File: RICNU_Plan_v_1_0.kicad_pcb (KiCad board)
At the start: 4 copper layers, 50 x 55 mm, 220 parts, among them J1 USB_OTG, J2 MOLEX-PC6, J3 DF52-4S-0.8H(21), J4 DF52-4S-0.8H(21), J5 MOLEX-PC20, J6 2x0.1, J7 FH19C-6S-0.5SH(05), Q1 N-CH, Q2 N-CH, SW1 CL-SB-12B-01T, SW2 SW_Push, SW3 SW_Push, U1 TPS2113, U2 TLV62568, U3 SN74AHC126, U4 FT232RL, U5 TCAN334G, U6 SN65HVD75, U7 BT121, U8 STM32F103RC, Y1 Crystal

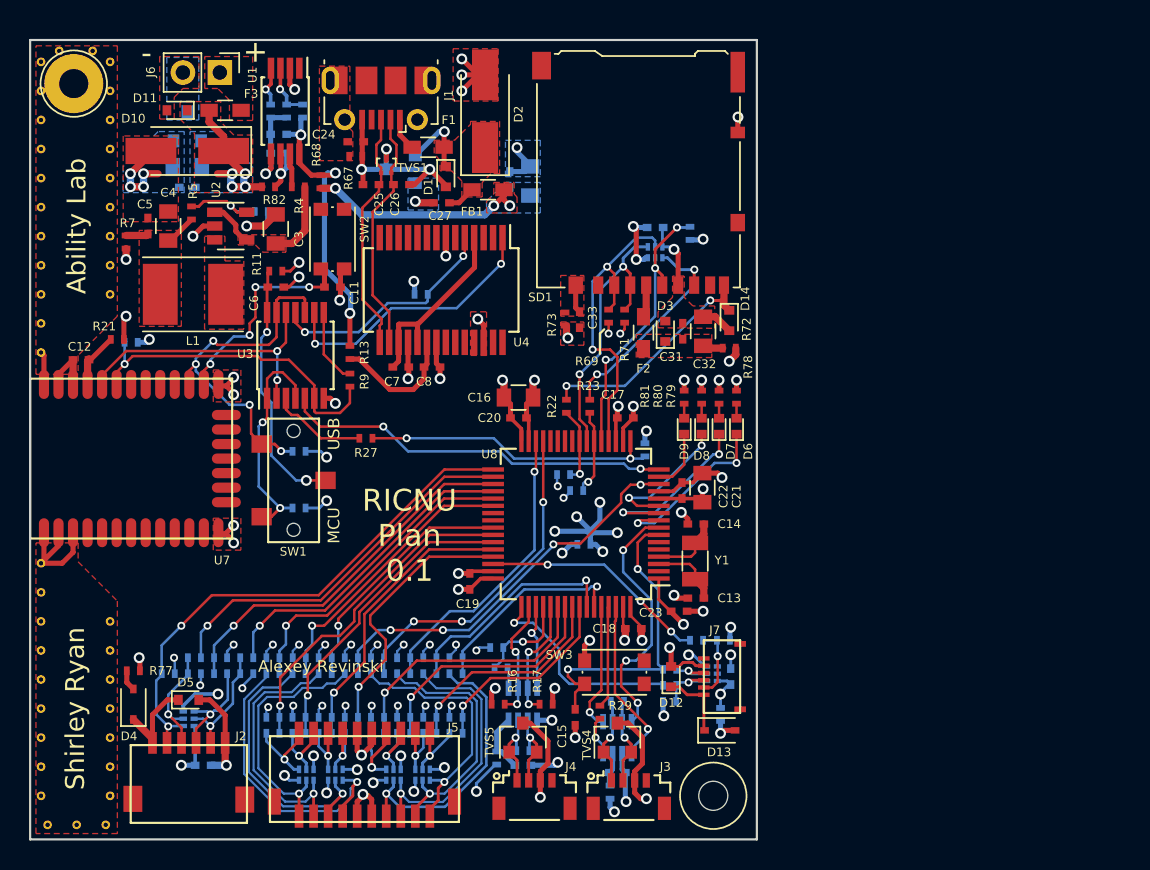
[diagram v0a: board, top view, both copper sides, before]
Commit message: Re-routed CAN, RS-485, and debug connectors (wrong polarity in all)
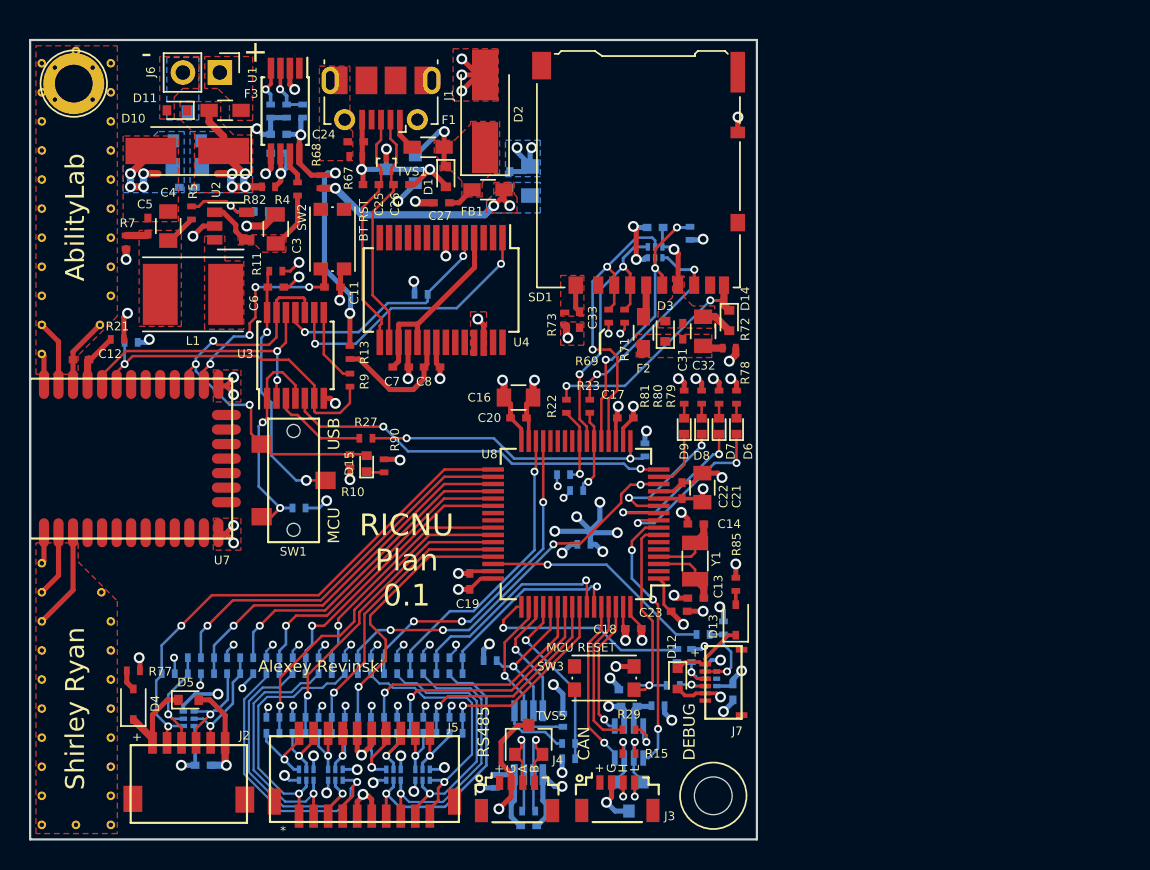
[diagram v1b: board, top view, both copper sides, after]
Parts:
- removed the REF** at (122.3, 94.5)
- removed the REF** at (127.1, 82.5)
- removed the REF** at (127.1, 84.5)
- removed the REF** at (127.1, 86.5)
- removed the REF** at (122.3, 86.5)
- removed the REF** at (122.3, 82.5)
- removed the REF** at (122.3, 84.5)
- removed the REF** at (127.1, 92.5)
- removed the REF** at (127.1, 94.5)
- removed the REF** at (127.1, 88.5)
- removed the REF** at (127.1, 90.5)
- removed the REF** at (122.3, 92.5)
- removed the REF** at (127.1, 78.5)
- removed the REF** at (122.3, 98.5)
- removed the REF** at (122.3, 96.5)
- removed the REF** at (122.3, 113.0)
- removed the REF** at (127.1, 117.0)
- removed the REF** at (127.1, 119.0)
- removed the REF** at (127.1, 129.0)
- removed the REF** at (127.1, 127.0)
- removed the REF** at (127.1, 125.0)
- removed the REF** at (127.1, 123.0)
- removed the REF** at (122.3, 90.5)
- removed the REF** at (127.1, 121.0)
- removed the REF** at (126.8, 131.0)
- removed the REF** at (124.8, 131.0)
- removed the REF** at (122.8, 131.0)
- removed the REF** at (122.3, 129.0)
- removed the REF** at (122.3, 127.0)
- removed the REF** at (122.3, 125.0)
- removed the REF** at (122.3, 123.0)
- removed the REF** at (122.3, 121.0)
- removed the REF** at (122.3, 119.0)
- removed the REF** at (122.3, 88.5)
- removed the REF** at (122.3, 117.0)
- removed the REF** at (122.3, 115.0)
- removed the REF** at (122.3, 78.5)
- removed the REF** at (122.3, 80.5)
- removed the REF** at (123.6, 77.8)
- removed the REF** at (125.9, 77.8)
- removed the REF** at (127.1, 80.5)
- added D15: LED, LEDs:LED_0402, F.Cu at (144.8, 106.2)
- added R90: R, Resistors_SMD:R_0402_NoSilk, F.Cu at (145.9, 106.3)
- added REF**: VIA-0.6-0.3, RICNU_Plan_v_1_0:VIA-0.6-0.3, F.Cu at (123.3, 81.1)
- added REF**: VIA-0.6-0.3, RICNU_Plan_v_1_0:VIA-0.6-0.3, F.Cu at (127.2, 92.6)
- added REF**: VIA-0.6-0.3, RICNU_Plan_v_1_0:VIA-0.6-0.3, F.Cu at (127.2, 94.6)
- added REF**: VIA-0.6-0.3, RICNU_Plan_v_1_0:VIA-0.6-0.3, F.Cu at (127.2, 90.6)
- added REF**: VIA-0.6-0.3, RICNU_Plan_v_1_0:VIA-0.6-0.3, F.Cu at (127.2, 86.6)
- added REF**: VIA-0.6-0.3, RICNU_Plan_v_1_0:VIA-0.6-0.3, F.Cu at (127.2, 88.6)
- added REF**: VIA-0.6-0.3, RICNU_Plan_v_1_0:VIA-0.6-0.3, F.Cu at (122.4, 78.6)
- added REF**: VIA-0.6-0.3, RICNU_Plan_v_1_0:VIA-0.6-0.3, F.Cu at (127.2, 78.6)
- added REF**: VIA-0.6-0.3, RICNU_Plan_v_1_0:VIA-0.6-0.3, F.Cu at (127.2, 80.6)
- added REF**: VIA-0.6-0.3, RICNU_Plan_v_1_0:VIA-0.6-0.3, F.Cu at (122.4, 98.6)
- added REF**: VIA-0.6-0.3, RICNU_Plan_v_1_0:VIA-0.6-0.3, F.Cu at (122.4, 96.6)
- added REF**: VIA-0.6-0.3, RICNU_Plan_v_1_0:VIA-0.6-0.3, F.Cu at (125.9, 81.1)
- added REF**: VIA-0.6-0.3, RICNU_Plan_v_1_0:VIA-0.6-0.3, F.Cu at (122.4, 94.6)
- added REF**: VIA-0.6-0.3, RICNU_Plan_v_1_0:VIA-0.6-0.3, F.Cu at (122.4, 92.6)
- added REF**: VIA-0.6-0.3, RICNU_Plan_v_1_0:VIA-0.6-0.3, F.Cu at (122.4, 90.6)
- added REF**: VIA-0.6-0.3, RICNU_Plan_v_1_0:VIA-0.6-0.3, F.Cu at (122.4, 84.6)
- added REF**: VIA-0.6-0.3, RICNU_Plan_v_1_0:VIA-0.6-0.3, F.Cu at (122.4, 82.6)
- added REF**: VIA-0.6-0.3, RICNU_Plan_v_1_0:VIA-0.6-0.3, F.Cu at (122.4, 86.6)
- added REF**: VIA-0.6-0.3, RICNU_Plan_v_1_0:VIA-0.6-0.3, F.Cu at (122.4, 88.6)
- added REF**: VIA-0.6-0.3, RICNU_Plan_v_1_0:VIA-0.6-0.3, F.Cu at (122.4, 80.6)
- added REF**: VIA-0.6-0.3, RICNU_Plan_v_1_0:VIA-0.6-0.3, F.Cu at (124.8, 131.0)
- added REF**: VIA-0.6-0.3, RICNU_Plan_v_1_0:VIA-0.6-0.3, F.Cu at (127.2, 131.0)
- added REF**: VIA-0.6-0.3, RICNU_Plan_v_1_0:VIA-0.6-0.3, F.Cu at (123.3, 78.9)
- added REF**: VIA-0.6-0.3, RICNU_Plan_v_1_0:VIA-0.6-0.3, F.Cu at (127.2, 129.0)
- added REF**: VIA-0.6-0.3, RICNU_Plan_v_1_0:VIA-0.6-0.3, F.Cu at (127.2, 127.0)
- added REF**: VIA-0.6-0.3, RICNU_Plan_v_1_0:VIA-0.6-0.3, F.Cu at (127.2, 125.0)
- added REF**: VIA-0.6-0.3, RICNU_Plan_v_1_0:VIA-0.6-0.3, F.Cu at (127.2, 123.0)
- added REF**: VIA-0.6-0.3, RICNU_Plan_v_1_0:VIA-0.6-0.3, F.Cu at (127.2, 121.0)
- added REF**: VIA-0.6-0.3, RICNU_Plan_v_1_0:VIA-0.6-0.3, F.Cu at (127.2, 119.0)
- added REF**: VIA-0.6-0.3, RICNU_Plan_v_1_0:VIA-0.6-0.3, F.Cu at (127.2, 117.0)
- added REF**: VIA-0.6-0.3, RICNU_Plan_v_1_0:VIA-0.6-0.3, F.Cu at (126.5, 115.0)
- added REF**: VIA-0.6-0.3, RICNU_Plan_v_1_0:VIA-0.6-0.3, F.Cu at (122.4, 131.0)
- added REF**: VIA-0.6-0.3, RICNU_Plan_v_1_0:VIA-0.6-0.3, F.Cu at (122.4, 129.0)
- added REF**: VIA-0.6-0.3, RICNU_Plan_v_1_0:VIA-0.6-0.3, F.Cu at (125.9, 78.9)
- added REF**: VIA-0.6-0.3, RICNU_Plan_v_1_0:VIA-0.6-0.3, F.Cu at (122.4, 127.0)
- added REF**: VIA-0.6-0.3, RICNU_Plan_v_1_0:VIA-0.6-0.3, F.Cu at (122.4, 125.0)
- added REF**: VIA-0.6-0.3, RICNU_Plan_v_1_0:VIA-0.6-0.3, F.Cu at (122.4, 123.0)
- added REF**: VIA-0.6-0.3, RICNU_Plan_v_1_0:VIA-0.6-0.3, F.Cu at (122.4, 121.0)
- added REF**: VIA-0.6-0.3, RICNU_Plan_v_1_0:VIA-0.6-0.3, F.Cu at (122.4, 119.0)
- added REF**: VIA-0.6-0.3, RICNU_Plan_v_1_0:VIA-0.6-0.3, F.Cu at (122.4, 117.0)
- added REF**: VIA-0.6-0.3, RICNU_Plan_v_1_0:VIA-0.6-0.3, F.Cu at (122.4, 115.0)
- added REF**: VIA-0.6-0.3, RICNU_Plan_v_1_0:VIA-0.6-0.3, F.Cu at (122.4, 113.0)
- added REF**: VIA-0.6-0.3, RICNU_Plan_v_1_0:VIA-0.6-0.3, F.Cu at (126.4, 96.6)
- added REF**: VIA-0.6-0.3, RICNU_Plan_v_1_0:VIA-0.6-0.3, F.Cu at (124.8, 77.8)
- added REF**: VIA-0.6-0.3, RICNU_Plan_v_1_0:VIA-0.6-0.3, F.Cu at (127.2, 84.6)
- added REF**: VIA-0.6-0.3, RICNU_Plan_v_1_0:VIA-0.6-0.3, F.Cu at (127.2, 82.6)
- C15, R16, R17, TVS4: moved to B.Cu
- R10, R15, R85: moved to F.Cu
- SW2, SW3: value SW_Push -> SW_Push_4pin; footprint Buttons_Switches_SMD:SW_SPST_KMR2 -> RICNU_Plan_v_1_0:SW_SPST_KMR7
- U6: footprint TO_SOT_Packages_SMD:SOT-23-8 -> Housings_SSOP:VSSOP-8_3.0x3.0mm_Pitch0.65mm
- moved R86 9.11 mm to (158.7, 126.5)
- moved R85 9.01 mm to (170.2, 114.5)
- moved D13 7.68 mm to (170.2, 116.9), turned to 90 degrees
- moved R28 6.98 mm to (158.7, 125.4), turned to 0 degrees
- moved R14 6.80 mm to (164.8, 122.8), turned to 180 degrees
- moved R17 4.88 mm to (153.2, 119.7), turned to 0 degrees
- moved C9 4.62 mm to (162.8, 122.8), turned to 180 degrees
- moved R16 4.58 mm to (158.2, 123.8), turned to 90 degrees
- moved C10 4.17 mm to (155.9, 131.1)
- moved R19 4.17 mm to (155.9, 130.1)
- moved TVS4 4.13 mm to (162.8, 129.1), turned to 270 degrees
- moved C15 4.03 mm to (162.7, 121.7), turned to 180 degrees
- moved R15 3.69 mm to (162.8, 126.1), turned to 0 degrees
- moved R10 3.56 mm to (143.6, 106.0), turned to 270 degrees
- moved R84 3.49 mm to (167.1, 119.3), turned to 90 degrees
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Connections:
- J3 pad 1: /CAN- -> Net-(J3-Pad1)
- J3 pad 2: /CAN+ -> GND
- J3 pad 3: GND -> /CAN+
- J3 pad 4: Net-(J3-Pad4) -> /CAN-
- J4 pad 1: /RS485_D- -> Net-(J4-Pad1)
- J4 pad 2: /RS485_D+ -> GND
- J4 pad 3: GND -> /RS485_D+
- J4 pad 4: Net-(J4-Pad4) -> /RS485_D-
- J7 pad 1: /Debug Connector/SWD_VREF -> Net-(J7-Pad1)
- J7 pad 2: /SWD_SWDIO -> GND
- J7 pad 3: /SWD_SWCLK -> /SWD_RESET
- J7 pad 4: /SWD_RESET -> /SWD_SWCLK
- J7 pad 5: GND -> /SWD_SWDIO
- J7 pad 6: Net-(J7-Pad6) -> /Debug Connector/SWD_VREF
- R19 pad 1: /RS485_D- -> /RS485_D+
- R19 pad 2: /RS485_D+ -> /RS485_D-
- TVS10 pad 1: /SWD_SWCLK -> /SWD_RESET
- TVS10 pad 2: /SWD_RESET -> /SWD_SWCLK
- TVS4 pad 1: /CAN- -> /CAN+
- TVS4 pad 2: /CAN+ -> /CAN-
- TVS5 pad 1: /RS485_D- -> /RS485_D+
- TVS5 pad 2: /RS485_D+ -> /RS485_D-
- U6 pad 6: /RS485_D+ -> /RS485_D-
- U6 pad 7: /RS485_D- -> /RS485_D+
- U8 pad 60: /CAN_SHDN -> /CAN_STB
- U8 pad 8: /CAN_STB -> /CAN_SHDN
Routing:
- net GND: track 147.7 -> 160.7 mm, vias 60 -> 63
- net /CAN_SHDN: track 8.83 -> 18.5 mm, vias 1 -> 3
- net /MCU/MCU_SWD_RESET: track 21.6 -> 15.3 mm, vias 2 -> 1
- net /CAN_STB: track 17.6 -> 11.5 mm, vias 3 -> 1
- net /MCU/MCU_RS485_RX: track 6.73 -> 12.4 mm
- net /BT_BOOT0: track 25.0 -> 30.2 mm, vias 4 -> 3
- net /RS485_RXE: track 8.25 -> 12.0 mm, vias 2 -> 1
- net /MCU/MCU_CAN_RX: track 7.12 -> 10.6 mm
- net /RS485_RX: track 1.43 -> 4.73 mm
- net /RS485_D+: track 5.55 -> 8.39 mm
- net /RS485_D-: track 5.55 -> 8.39 mm
- net /RS485_TX: track 5.88 -> 8.51 mm
- net /CAN_TX: track 11.5 -> 9.36 mm
- net +3V3: track 55.3 -> 57.0 mm, vias 48 -> 49
- net /RS485_TXE: track 8.42 -> 10.1 mm, vias 2 -> 1
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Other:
- board text added: "*"
- board text added: "A"
- board text added: "AbilityLab"
- board text added: "B"
- board text added: "BT RST"
- board text added: "CAN"
- board text added: "DEBUG"
- board text added: "G"
- board text added: "H"
- board text added: "L"
- board text added: "MCU RESET"
- board text added: "RS485"
- board text removed: "Ability Lab"

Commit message: Added connections to monitor power, changed CANSTB MCU pin, moved LED pins around
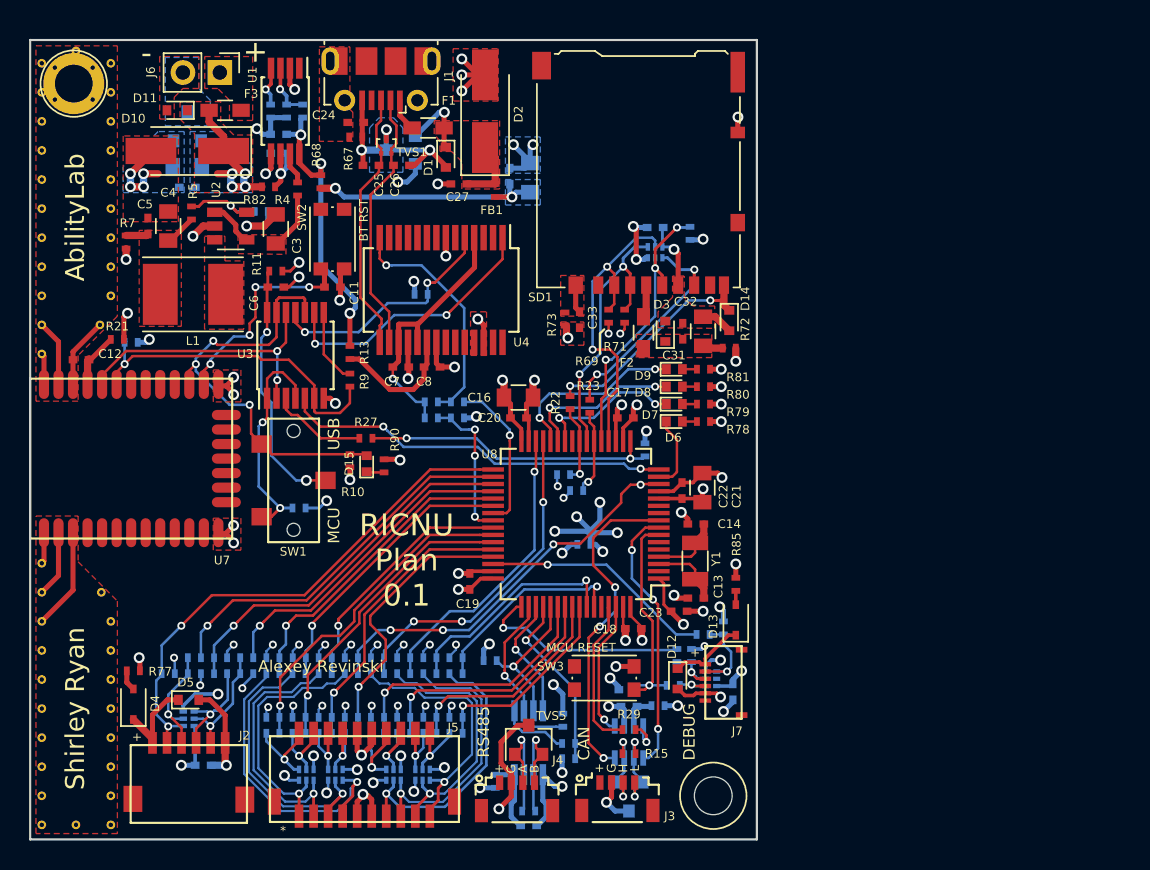
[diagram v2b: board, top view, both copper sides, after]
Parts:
- added R91: 10k, Resistors_SMD:R_0402_NoSilk, B.Cu at (149.2, 101.9)
- added R92: 10k, Resistors_SMD:R_0402_NoSilk, B.Cu at (151.0, 103.0)
- added R93: 180, Resistors_SMD:R_0402_NoSilk, B.Cu at (151.0, 101.9)
- added R94: 180, Resistors_SMD:R_0402_NoSilk, B.Cu at (149.2, 103.0)
- D1, D11: value TVS -> 5.0V TVS
- D12, D14, D3, D5: value TVS -> 3.3V TVS
- FB1: footprint Resistors_SMD:R_0603_HandSoldering -> Resistors_SMD:R_0402_NoSilk
- moved D6 4.28 mm to (165.9, 103.2), turned to 0 degrees
- moved D9 3.98 mm to (165.9, 99.7), turned to 0 degrees
- moved D7 3.43 mm to (165.9, 102.0), turned to 0 degrees
- moved D8 3.30 mm to (165.9, 100.8), turned to 0 degrees
- moved R78 2.82 mm to (167.9, 103.2), turned to 180 degrees
- moved R81 2.34 mm to (167.9, 99.7), turned to 180 degrees
- moved C27 1.77 mm to (151.1, 86.9)
- moved D1 1.33 mm to (150.2, 85.1)
- moved Q1 1.33 mm to (147.1, 84.6)
- moved C24 1.33 mm to (144.0, 82.7)
- moved C25 1.33 mm to (145.1, 85.6)
- moved C26 1.33 mm to (147.2, 85.6)
- moved F1 1.33 mm to (149.0, 83.0)
- moved J1 1.33 mm to (145.7, 78.8)
- moved R67 1.33 mm to (144.0, 83.7)
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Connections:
- net /USB to UART/3V3FTDI renamed /FTDI_USBON
- D15 pad 2: /BT_BOOT0 -> /BT_UART_TX
- R10 pad 1: /BT_BOOT0 -> /BT_UART_TX
- R20 pad 2: /BT_UART_RX -> /Bluetooth/BT.RX
- R9 pad 2: /BT_UART_RX -> /Bluetooth/BT.RX
- SW1 pad 1: /BT_BOOT0 -> /BT_UART_TX
- U3 pad 10: /BT_BOOT0 -> /BT_UART_TX
- U3 pad 12: /BT_UART_TX -> /BT_UART_RX
- U3 pad 13: /BT_BOOT0 -> /BT_UART_TX
- U3 pad 2: /BT_UART_TX -> /BT_UART_RX
- U3 pad 6: /BT_UART_RX -> /Bluetooth/BT.RX
- U4 pad 14: Net-(U4-Pad14) -> /FTDI_PWREN
- U7 pad 23: /BT_BOOT0 -> /BT_UART_TX
- U7 pad 28: /BT_UART_RX -> /Bluetooth/BT.RX
- U7 pad 29: /BT_UART_TX -> /BT_UART_RX
- U8 pad 10: /LED2 -> Net-(U8-Pad10)
- U8 pad 11: /LED3 -> Net-(U8-Pad11)
- U8 pad 15: /LED4 -> /LED1
- U8 pad 26: Net-(U8-Pad26) -> /LED2
- U8 pad 27: Net-(U8-Pad27) -> /LED3
- U8 pad 28: Net-(U8-Pad28) -> /LED4
- U8 pad 39: Net-(U8-Pad39) -> /MCU/MCU_PWREN
- U8 pad 40: Net-(U8-Pad40) -> /MCU/MCU_USBON
- U8 pad 60: /CAN_STB -> Net-(U8-Pad60)
- U8 pad 9: /LED1 -> /CAN_STB
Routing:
- net /BT_BOOT0: track 30.2 -> 0.00 mm, vias 3 -> 0
- net /Bluetooth/BT.RX: track 0.00 -> 24.6 mm, vias 0 -> 1
- net /FTDI_PWREN: track 0.00 -> 16.4 mm, vias 0 -> 1
- net /CAN_STB: track 11.5 -> 23.1 mm, vias 1 -> 3
- net /MCU/MCU_PWREN: track 0.00 -> 10.7 mm, vias 0 -> 1
- net /BT_UART_TX: track 19.6 -> 30.2 mm, vias 2 -> 3
- net /MCU/MCU_USBON: track 0.00 -> 10.3 mm, vias 0 -> 3
- net /LED4: track 4.19 -> 12.6 mm, vias 0 -> 2
- net /LED1: track 12.0 -> 5.16 mm, vias 2 -> 0
- net /BT_UART_RX: track 24.6 -> 19.6 mm, vias 1 -> 2
- net /FTDI_USBON: track 13.2 -> 18.0 mm, vias 0 -> 1
- net /USB Connector/VBUS_PROTECTED: track 7.06 -> 9.88 mm
- net /LED2: track 12.1 -> 10.2 mm
- net +3V3: track 57.0 -> 55.4 mm
- net /LED3: track 9.55 -> 11.2 mm
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- added copper zone on B.Cu, net /USB Connector/GND_USB_CABLE
- removed copper zone on F.Cu, net /USB Connector/VBUS_PROTECTED_FILTERED

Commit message: had to relocate 4.7uF cap for STM32 based on datasheet info. Experimenting with reset button location
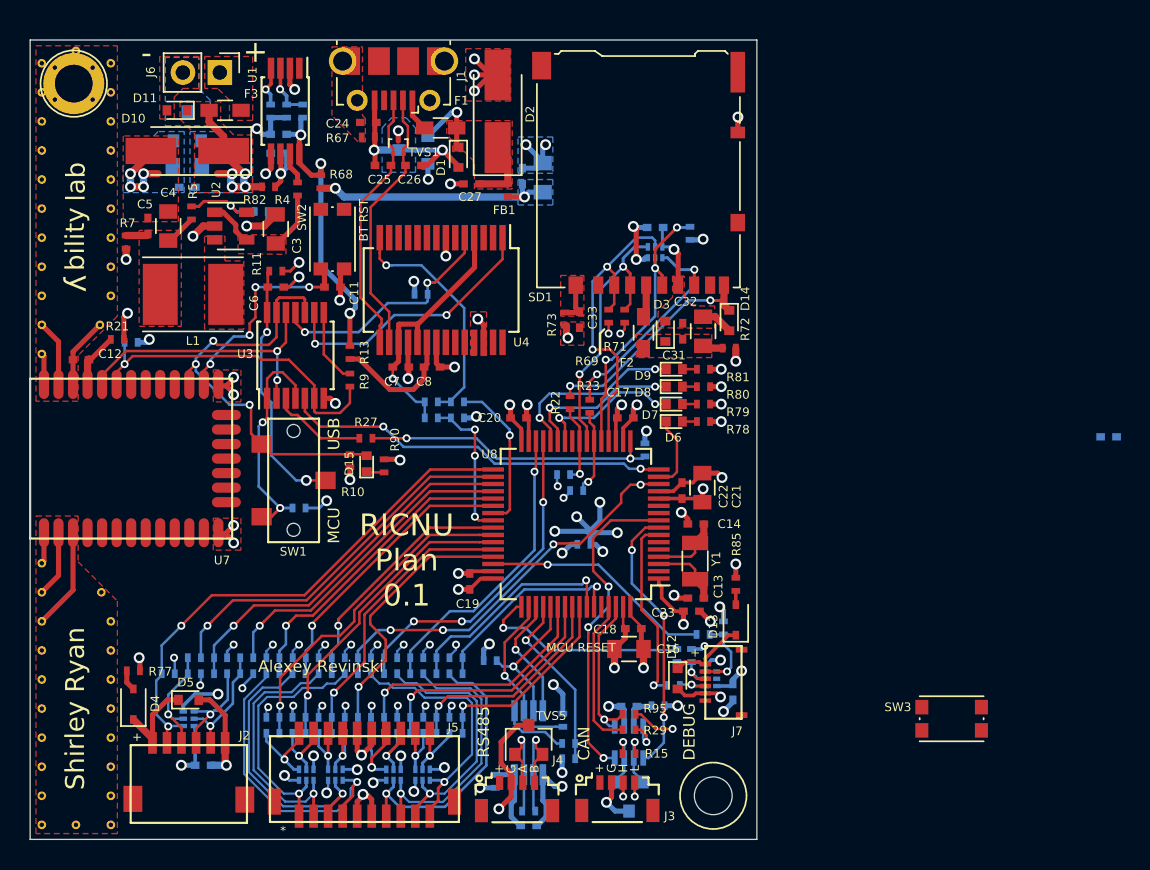
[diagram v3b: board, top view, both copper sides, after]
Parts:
- added R95: 10k, Resistors_SMD:R_0402_NoSilk, F.Cu at (162.8, 123.4)
- J1: footprint Connectors_USB:USB_Micro-B_Molex-105017-0001 -> USB_Micro-B_Molex-105017-0001
- moved C15 37.4 mm to (195.8, 104.3)
- moved SW3 24.1 mm to (185.0, 123.7)
- moved C16 18.9 mm to (162.8, 118.9), turned to 180 degrees
- moved C24 0.87 mm to (144.9, 82.7)
- moved C27 0.87 mm to (152.0, 86.9)
- moved C28 0.87 mm to (155.5, 86.4)
- moved C29 0.87 mm to (156.9, 86.5)
- moved D1 0.87 mm to (151.1, 85.1)
- moved F1 0.87 mm to (149.8, 83.0)
- moved FB1 0.87 mm to (154.5, 87.3)
- moved Q1 0.87 mm to (148.0, 84.6)
- moved R67 0.87 mm to (144.9, 83.7)
- moved D2 0.86 mm to (153.8, 81.9)
- moved J1 0.86 mm to (146.6, 78.8)
- moved C23 0.85 mm to (167.1, 116.3)
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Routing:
- net GND: track 162.0 -> 158.8 mm, vias 64 -> 62
- net +3V3: track 55.4 -> 58.3 mm, vias 49 -> 50
- net /MCU/MCU_SWD_RESET: track 15.3 -> 12.9 mm
- net /USB Connector/GND_USB_CABLE: track 15.0 -> 13.6 mm
- net /CAN_TX: track 9.36 -> 10.8 mm
- net /SD Card Socket/SD_SHIELD: track 1.94 -> 2.96 mm
- net /USB Connector/VBUS_PROTECTED_FILTERED: track 16.9 -> 17.8 mm
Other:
- board text added: "bility"
- board text added: "lab"
- board text added: "y"
- board text removed: "AbilityLab"
